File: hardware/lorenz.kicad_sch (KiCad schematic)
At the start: 87 parts, among them J1 USB-C, J2 BNC, J3 BNC, J4 BNC, J5 BNC, SW1 SW_DIP_x06, U1 LF412, U2 LF412, U3 MPY634, U4 MPY634, U5 A0515S-2WR2, U6 78L12, U7 79L12

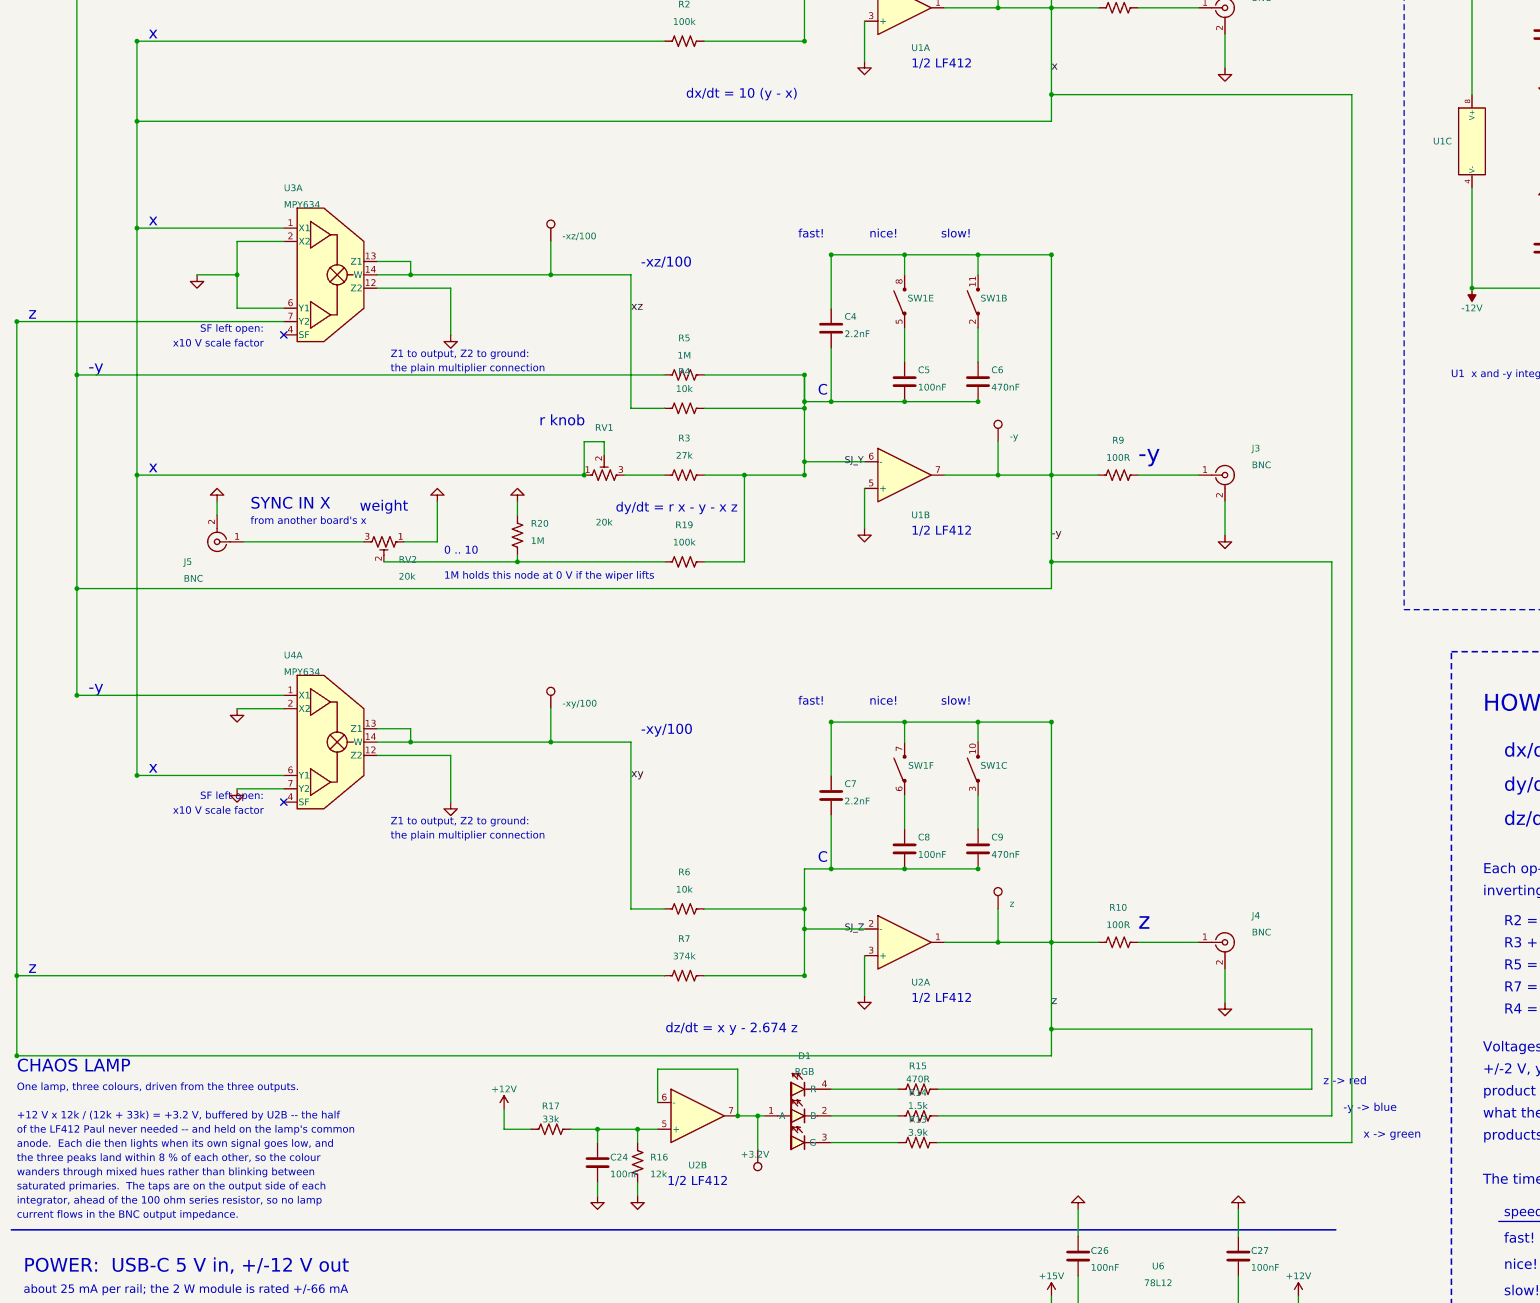
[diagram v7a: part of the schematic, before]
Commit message: Rev B: build the top-scoring chaos lamp, and clear J1's silk from the edge
The lamp becomes candidate 1 of docs/lamp2: common anode at +3.75 V
(R16 15k), red fed from -y through 1.5k with x blended in through 8.2k
and +12 V through 8.2k, green from x through 24k, blue from z through
2.2k with -12 V through 36k.  Three resistors more than rev A, all
JLCPCB Basic parts; D1's footprint, place and angle are rev A's, which
its boards proved.  The symbol draws the dies blue, red, green so the
schematic's feeds still never cross.

check_circuit.py now reads the lamp back out of the netlist, checks it
is that wiring, and simulates it with the corrected LED model: 0.82 at
slow!, against rev A's 0.33.  Everything outside the lamp was compared
with rev A: all 204 other pins wire identically, the outline and
non-plated holes are byte-identical, and every routed net but the
lamp's and /SJ_Y (re-routed 1.2 mm lower near U1) is unchanged.

Also:
  * J1's silk stubs ended 0.15 mm from the edge, inside JLCPCB's 0.2 mm
    pull-back; trimmed to 0.45 mm.
  * The schematic checker now models KiCad reversing justification on
    rotated symbols' fields -- it had let six clashing labels through.
  * The eye filter is plain numpy again, so ./make.py needs only numpy
    and Pillow, as the README says.
  * The assembler notes gave D1's pin order as anticlockwise; it is
    clockwise.
  * Op-amp values hidden like the multipliers': "LF412 op-amp" says it.
  * Stock refreshed for the scarce parts; rev B, dated 2026-10-02.

Co-Authored-By: Claude Opus 5.5 <noreply@anthropic.com>
Claude-Session: https://claude.ai/code/session_01FyYQ1p4JtCVvJKRozbkYm7
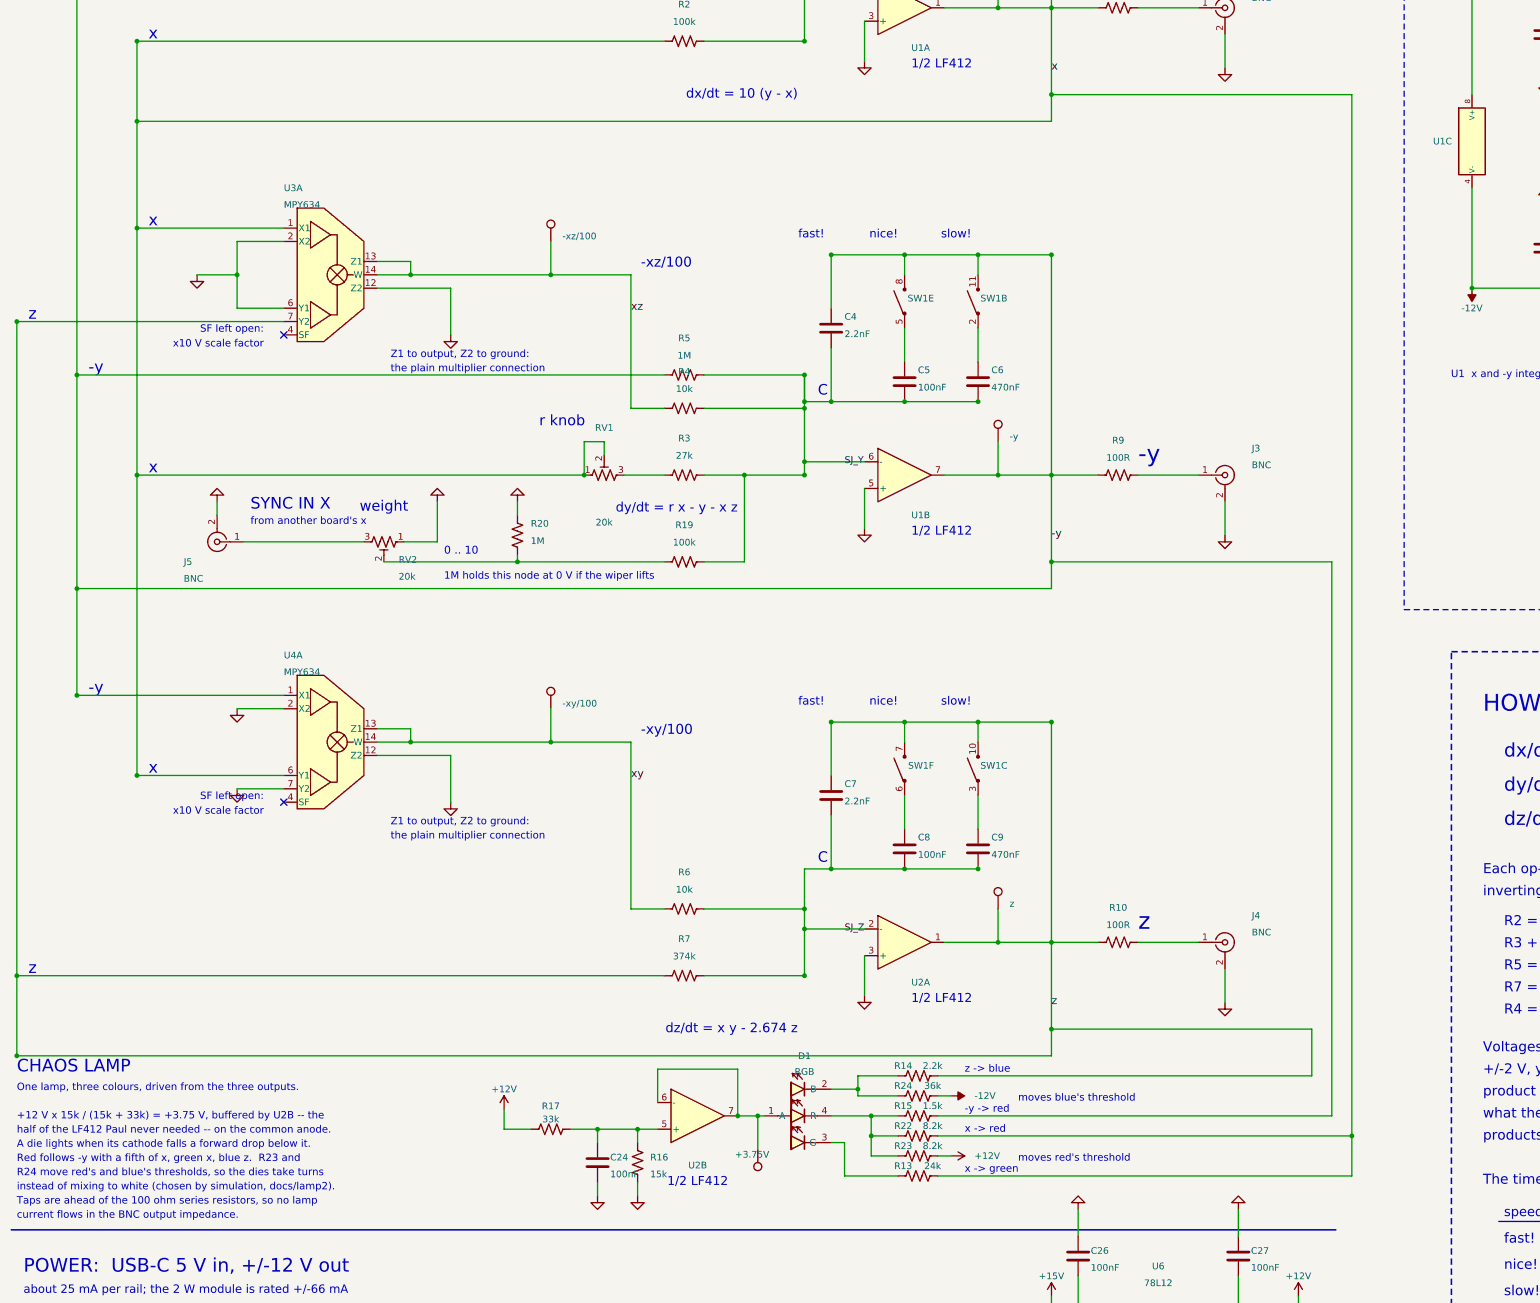
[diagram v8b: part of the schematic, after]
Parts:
- added R22, R23: 8.2k, Resistor_SMD:R_0805_2012Metric, symbol Device:R_US
- added R24: 36k, Resistor_SMD:R_0805_2012Metric, symbol Device:R_US
- R13: value 3.9k -> 24k; LCSC C17614 -> C17575; MPN 0805W8F3901T5E -> 0805W8F2402T5E
- R14: value 1.5k -> 2.2k; LCSC C4310 -> C17520; MPN 0805W8F1501T5E -> 0805W8F2201T5E
- R15: value 470R -> 1.5k; LCSC C17710 -> C4310; MPN 0805W8F4700T5E -> 0805W8F1501T5E
- R16: value 12k -> 15k; LCSC C17444 -> C17475; MPN 0805W8F1202T5E -> 0805W8F1502T5E
- TP6: value +3.2V -> +3.75V
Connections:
- net +12V: now also R23.2
- net -12V: now also R24.2
- net -y: now also R15.2; no longer R14.2
- net x: now also R22.2
- net z: now also R14.2; no longer R15.2
- net at D1.4 (R), R15.1: now also R22.1, R23.1
- net at D1.2 (B), R14.1: now also R24.1
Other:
- note added: "+12 V x 15k / (15k + 33k) = +3.75 V, buffered by U2B -- the"
- note added: "-y -> red"
- note added: "A die lights when its cathode falls a forward drop below it."
- note added: "R24 move red's and blue's thresholds, so the dies take turns"
- note added: "Red follows -y with a fifth of x, green x, blue z. R23 and"
- note added: "Taps are ahead of the 100 ohm series resistors, so no lamp"
- note added: "half of the LF412 Paul never needed -- on the common anode."
- note added: "instead of mixing to white (chosen by simulation, docs/lamp2)."
- note added: "moves blue's threshold"
- note added: "moves red's threshold"
- note added: "x -> red"
- note added: "z -> blue"
- note removed: "+12 V x 12k / (12k + 33k) = +3.2 V, buffered by U2B -- the half"
- note removed: "-y -> blue"
- note removed: "anode. Each die then lights when its own signal goes low, and"
- note removed: "integrator, ahead of the 100 ohm series resistor, so no lamp"
- note removed: "of the LF412 Paul never needed -- and held on the lamp's common"
- note removed: "saturated primaries. The taps are on the output side of each"
- note removed: "the three peaks land within 8 % of each other, so the colour"
- note removed: "wanders through mixed hues rather than blinking between"
- note removed: "z -> red"
- moved on the sheet: R13, R14, R15
